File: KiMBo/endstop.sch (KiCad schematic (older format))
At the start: 19 parts

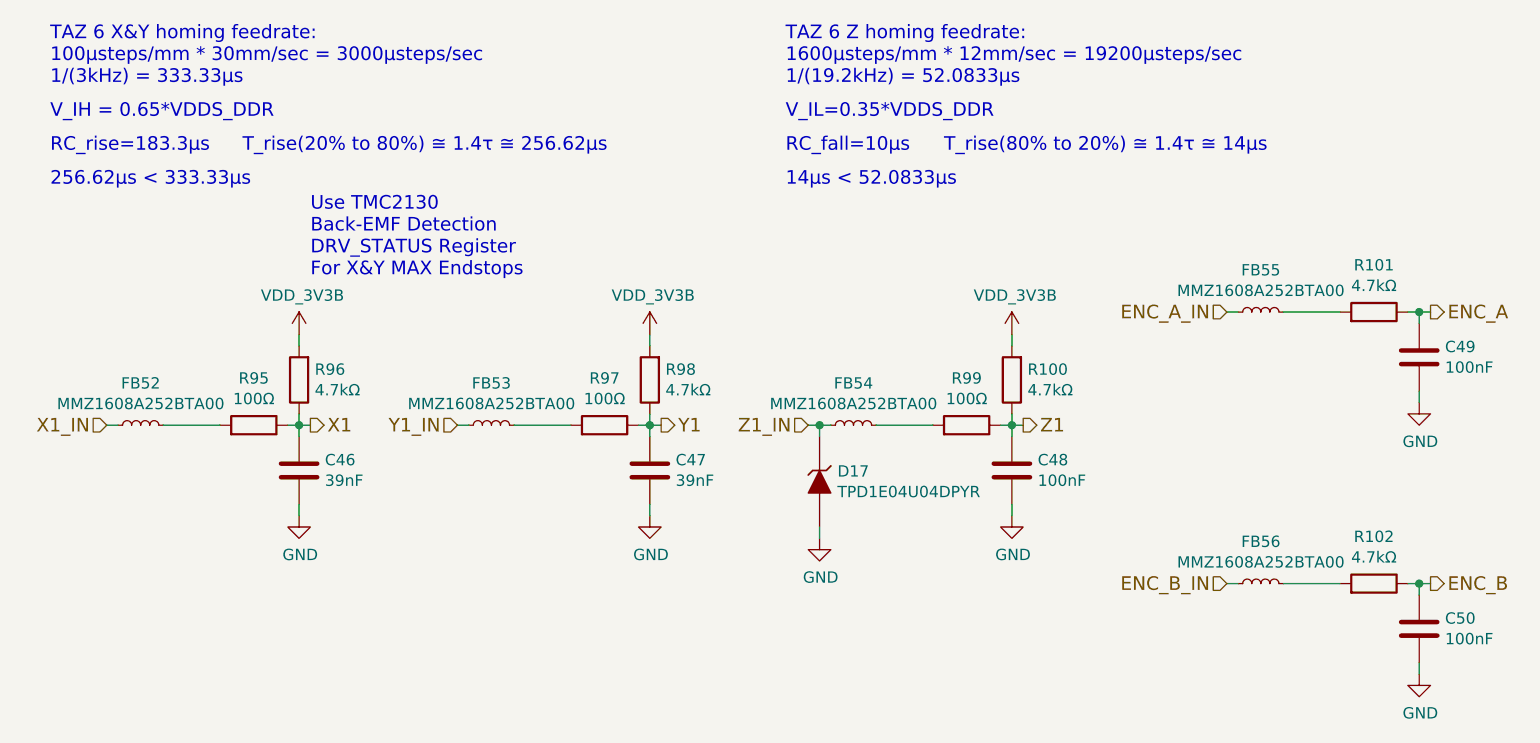
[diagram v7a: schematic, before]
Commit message: Routing open-drain output inverters, SOT-5 I2C EEPROM, begin adding bypass caps around the eMMC
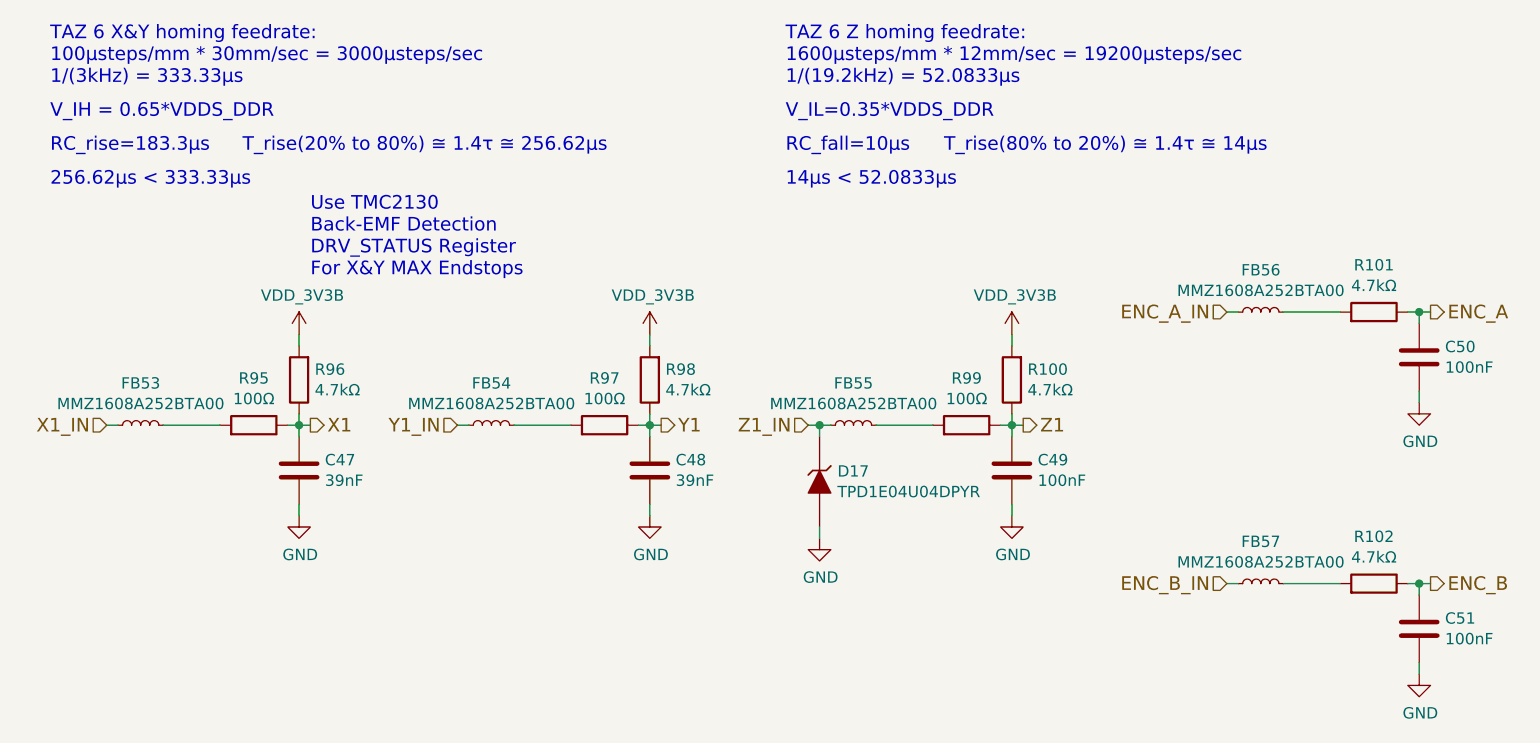
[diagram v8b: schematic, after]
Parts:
- renumbered C46 to C47, C47 to C48, C48 to C49, C49 to C50, C50 to C51, FB52 to FB53, FB53 to FB54, FB54 to FB55, FB55 to FB56, FB56 to FB57
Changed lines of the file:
@@
 X1
 $Comp
-L C C46
+L C C47
 U 1 1 58129032
 P 6150 5500
-F 0 "C46" H 6264 5546 50  0000 L CNN
+F 0 "C47" H 6264 5546 50  0000 L CNN
 F 1 "39nF" H 6264 5455 50  0000 L CNN
 F 2 "Capacitors_SMD:C_0603" H 6188 5350 50  0001 C CNN
@@
 Y1
 $Comp
-L C C47
+L C C48
 U 1 1 589415E7
 P 7700 5500
-F 0 "C47" H 7814 5546 50  0000 L CNN
+F 0 "C48" H 7814 5546 50  0000 L CNN
 F 1 "39nF" H 7814 5455 50  0000 L CNN
 F 2 "Capacitors_SMD:C_0603" H 7738 5350 50  0001 C CNN
@@
 Z1
 $Comp
-L C C48
+L C C49
 U 1 1 58941879
 P 9300 5500
-F 0 "C48" H 9414 5546 50  0000 L CNN
+F 0 "C49" H 9414 5546 50  0000 L CNN
 F 1 "100nF" H 9414 5455 50  0000 L CNN
 F 2 "Capacitors_SMD:C_0603" H 9338 5350 50  0001 C CNN
@@
 ENC_A
 $Comp
-L C C49
+L C C50
 U 1 1 5894C248
 P 11100 5000
-F 0 "C49" H 11214 5046 50  0000 L CNN
+F 0 "C50" H 11214 5046 50  0000 L CNN
 F 1 "100nF" H 11214 4955 50  0000 L CNN
 F 2 "Capacitors_SMD:C_0603" H 11138 4850 50  0001 C CNN
@@
 	11100 6000 11100 6050
 $Comp
-L C C50
+L C C51
 U 1 1 5894C2A4
 P 11100 6200
-F 0 "C50" H 11214 6246 50  0000 L CNN
+F 0 "C51" H 11214 6246 50  0000 L CNN
 F 1 "100nF" H 11214 6155 50  0000 L CNN
 F 2 "Capacitors_SMD:C_0603" H 11138 6050 50  0001 C CNN
@@
 ENC_B_IN
 $Comp
-L VDD_3V3B #PWR0144
+L VDD_3V3B #PWR0145
 U 1 1 59E67523
 P 6150 4900
-F 0 "#PWR0144" H 6150 4750 50  0001 C CNN
+F 0 "#PWR0145" H 6150 4750 50  0001 C CNN
 F 1 "VDD_3V3B" H 6165 5073 50  0000 C CNN
 F 2 "" H 6150 4900 50  0000 C CNN
@@
 $EndComp
 $Comp
-L VDD_3V3B #PWR0145
+L VDD_3V3B #PWR0146
 U 1 1 59E6755C
 P 7700 4900
-F 0 "#PWR0145" H 7700 4750 50  0001 C CNN
+F 0 "#PWR0146" H 7700 4750 50  0001 C CNN
 F 1 "VDD_3V3B" H 7715 5073 50  0000 C CNN
 F 2 "" H 7700 4900 50  0000 C CNN
@@
 $EndComp
 $Comp
-L VDD_3V3B #PWR0146
+L VDD_3V3B #PWR0147
 U 1 1 59E6758E
 P 9300 4900
-F 0 "#PWR0146" H 9300 4750 50  0001 C CNN
+F 0 "#PWR0147" H 9300 4750 50  0001 C CNN
 F 1 "VDD_3V3B" H 9315 5073 50  0000 C CNN
 F 2 "" H 9300 4900 50  0000 C CNN
@@
 	11050 6000 11150 6000
 $Comp
-L GND #PWR0147
+L GND #PWR0148
 U 1 1 59E68F88
 P 11100 5200
-F 0 "#PWR0147" H 11100 4950 50  0001 C CNN
+F 0 "#PWR0148" H 11100 4950 50  0001 C CNN
 F 1 "GND" H 11105 5027 50  0000 C CNN
 F 2 "" H 11100 5200 50  0000 C CNN
@@
 $EndComp
 $Comp
-L GND #PWR0148
+L GND #PWR0149
 U 1 1 59E68FBB
 P 11100 6400
-F 0 "#PWR0148" H 11100 6150 50  0001 C CNN
+F 0 "#PWR0149" H 11100 6150 50  0001 C CNN
 F 1 "GND" H 11105 6227 50  0000 C CNN
 F 2 "" H 11100 6400 50  0000 C CNN
@@
 $EndComp
 $Comp
-L GND #PWR0149
+L GND #PWR0150
 U 1 1 59E68FE7
 P 9300 5700
-F 0 "#PWR0149" H 9300 5450 50  0001 C CNN
+F 0 "#PWR0150" H 9300 5450 50  0001 C CNN
 F 1 "GND" H 9305 5527 50  0000 C CNN
 F 2 "" H 9300 5700 50  0000 C CNN
@@
 $EndComp
 $Comp
-L GND #PWR0150
+L GND #PWR0151
 U 1 1 59E69013
 P 7700 5700
-F 0 "#PWR0150" H 7700 5450 50  0001 C CNN
+F 0 "#PWR0151" H 7700 5450 50  0001 C CNN
 F 1 "GND" H 7705 5527 50  0000 C CNN
 F 2 "" H 7700 5700 50  0000 C CNN
@@
 $EndComp
 $Comp
-L GND #PWR0151
+L GND #PWR0152
 U 1 1 59E6903F
 P 6150 5700
-F 0 "#PWR0151" H 6150 5450 50  0001 C CNN
+F 0 "#PWR0152" H 6150 5450 50  0001 C CNN
 F 1 "GND" H 6155 5527 50  0000 C CNN
 F 2 "" H 6150 5700 50  0000 C CNN
@@
 	7100 5300 7350 5300
 $Comp
-L INDUCTOR_Small FB52
+L INDUCTOR_Small FB53
 U 1 1 5B28F416
 P 5450 5300
-F 0 "FB52" V 5635 5300 50  0000 C CNN
+F 0 "FB53" V 5635 5300 50  0000 C CNN
 F 1 "MMZ1608A252BTA00" V 5544 5300 50  0000 C CNN
 F 2 "KiMBo:Ferrite_Bead_0603" H 5450 5300 50  0001 C CNN
@@
 	5550 5300 5800 5300
 $Comp
-L INDUCTOR_Small FB55
+L INDUCTOR_Small FB56
 U 1 1 5B292FBD
 P 10400 4800
-F 0 "FB55" V 10585 4800 50  0000 C CNN
+F 0 "FB56" V 10585 4800 50  0000 C CNN
 F 1 "MMZ1608A252BTA00" V 10494 4800 50  0000 C CNN
 F 2 "KiMBo:Ferrite_Bead_0603" H 10400 4800 50  0001 C CNN
@@
 $EndComp
 $Comp
-L INDUCTOR_Small FB56
+L INDUCTOR_Small FB57
 U 1 1 5B293036
 P 10400 6000
-F 0 "FB56" V 10585 6000 50  0000 C CNN
+F 0 "FB57" V 10585 6000 50  0000 C CNN
 F 1 "MMZ1608A252BTA00" V 10494 6000 50  0000 C CNN
 F 2 "KiMBo:Ferrite_Bead_0603" H 10400 6000 50  0001 C CNN
@@
 Connection ~ 8450 5300
 $Comp
-L GND #PWR0152
+L GND #PWR0153
 U 1 1 5B4EDFC5
 P 8450 5800
-F 0 "#PWR0152" H 8450 5550 50  0001 C CNN
+F 0 "#PWR0153" H 8450 5550 50  0001 C CNN
 F 1 "GND" H 8455 5627 50  0000 C CNN
 F 2 "" H 8450 5800 50  0000 C CNN
@@
 	8450 5800 8450 5750
 $Comp
-L INDUCTOR_Small FB53
+L INDUCTOR_Small FB54
 U 1 1 5B9752EE
 P 7000 5300
-F 0 "FB53" V 7185 5300 50  0000 C CNN
+F 0 "FB54" V 7185 5300 50  0000 C CNN
 F 1 "MMZ1608A252BTA00" V 7094 5300 50  0000 C CNN
 F 2 "KiMBo:Ferrite_Bead_0603" H 7000 5300 50  0001 C CNN
@@
 $EndComp
 $Comp
-L INDUCTOR_Small FB54
+L INDUCTOR_Small FB55
 U 1 1 5B975719
 P 8600 5300
-F 0 "FB54" V 8785 5300 50  0000 C CNN
+F 0 "FB55" V 8785 5300 50  0000 C CNN
 F 1 "MMZ1608A252BTA00" V 8694 5300 50  0000 C CNN
 F 2 "KiMBo:Ferrite_Bead_0603" H 8600 5300 50  0001 C CNN
